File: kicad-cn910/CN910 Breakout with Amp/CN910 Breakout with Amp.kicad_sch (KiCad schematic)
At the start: 6 parts, among them J1 CN910_FPC_CON, J2 PB_RF_OUT

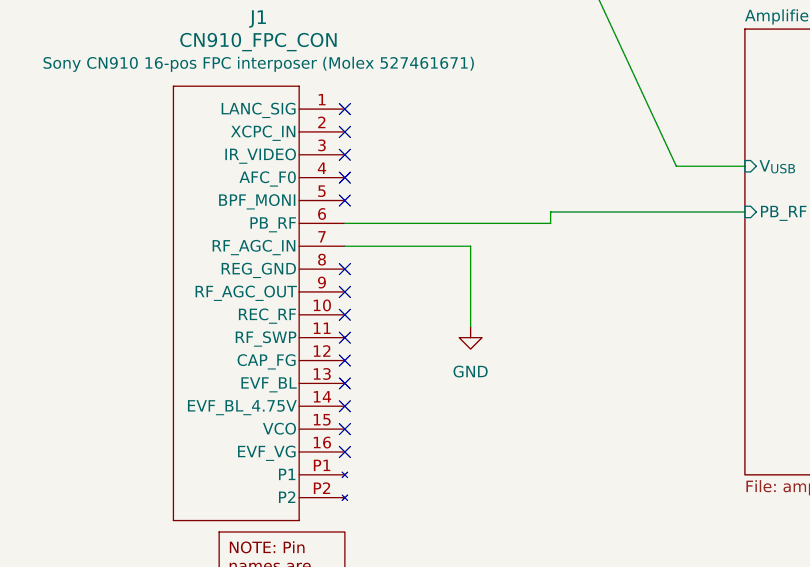
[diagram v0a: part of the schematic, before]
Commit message: Fixed CN910 pin 7/8 routing in the breakout with amp design. RF_AGC_IN (pin 7) was mistakenly tied to GND instead of REG_GND (pin 8).
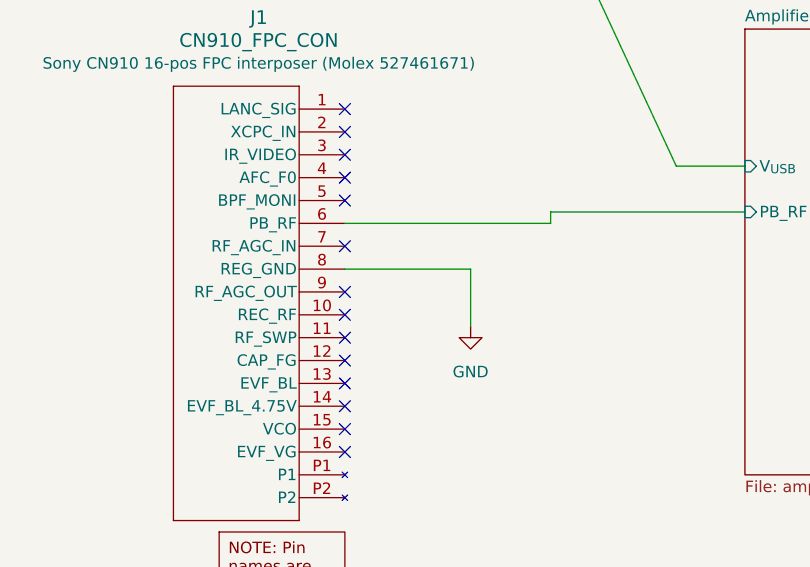
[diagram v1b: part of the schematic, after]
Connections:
- net GND: now also J1.8 (REG_GND); no longer J1.7 (RF_AGC_IN)
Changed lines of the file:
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@@
+	)
+	(no_connect
+		(at 55.88 115.57)
 	)
 	(no_connect
 		(at 55.88 107.95)
-	)
-	(no_connect
-		(at 55.88 118.11)
 	)
 	(no_connect
@@
 		(pts
 			(xy 78.74 113.03) (xy 78.74 111.76)
+		)
+		(stroke
+			(width 0)
+			(type default)
+		)
+	)
+	(wire
+		(pts
+			(xy 55.88 118.11) (xy 69.85 118.11)
 		)
 		(stroke
@@
 	(wire
 		(pts
-			(xy 69.85 115.57) (xy 69.85 124.46)
+			(xy 69.85 118.11) (xy 69.85 124.46)
 		)
 		(stroke
@@
 		)
 		(stroke
-			(width 0)
-			(type default)
-		)
-	)
-	(wire
-		(pts
-			(xy 55.88 115.57) (xy 69.85 115.57)
-		)
-		(stroke
